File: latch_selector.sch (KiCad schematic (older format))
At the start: 15 parts, among them SW1 SW_Coded_Octal-8, U1 74HCT138, U2 74HCT151, U6 74HCT32

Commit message: added diode-AND to unused latch select pins
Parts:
- removed D1: BAT54AW, Package_TO_SOT_SMD:SOT-323_SC-70, symbol Diode:BAT54AW
- added D1: SD103ATW, Package_TO_SOT_SMD:SOT-363_SC-70-6, symbol Diode:SD103ATW
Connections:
- wire segments 66 -> 65
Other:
- moved on the sheet: RN1
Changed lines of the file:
@@
-	1    0    0    -1
-$EndComp
-$Comp
-L rc2014_monitor-rescue:74HCT138-74xx U?
-U 1 1 5CC19E52
-P 2650 1700
-AR Path="/5CC19E52" Ref="U?"  Part="1"
-AR Path="/5CBDBC11/5CC19E52" Ref="U1"  Part="1"
-F 0 "U1" H 2650 1750 50  0000 C CNN
-F 1 "74HCT138" H 2600 1650 50  0000 C CNN
-F 2 "Package_DIP:DIP-16_W7.62mm" H 2650 1700 50  0001 C CNN
-F 3 "http://www.ti.com/lit/ds/symlink/cd74hct138.pdf" H 2650 1700 50  0001 C CNN
-F 4 "Texas Instruments" H -850 -2150 50  0001 C CNN "MFR"
-F 5 "SN74HCT138N" H -850 -2150 50  0001 C CNN "MPN"
-F 6 "Mouser" H -850 -2150 50  0001 C CNN "SPR"
-F 7 "595-SN74HCT138N" H -850 -2150 50  0001 C CNN "SPN"
-F 8 "-" H -850 -2150 50  0001 C CNN "SPURL"
-	1    2650 1700
 	1    0    0    -1
 $EndComp
@@
 M_WR
 Wire Wire Line
-	4000 1400 4200 1400
-Wire Wire Line
-	4000 1500 4200 1500
-Wire Wire Line
-	4000 1600 4200 1600
-Wire Wire Line
-	4000 1700 4200 1700
-Wire Wire Line
-	4000 1800 4200 1800
-Wire Wire Line
 	2650 1000 2650 1100
 Wire Wire Line
@@
 	2000 4850 2650 4850
 Wire Wire Line
-	4700 1400 4600 1400
+	4800 1400 4700 1400
 Wire Wire Line
 	2050 1000 2050 1900
@@
 Wire Wire Line
 	900  4350 2150 4350
-Wire Wire Line
-	2150 2000 2150 2100
-Wire Wire Line
-	2150 2400 2150 2100
 Connection ~ 2650 1000
 Connection ~ 2000 3850
@@
 Connection ~ 2000 4550
 Connection ~ 2650 4850
-Connection ~ 2650 2400
-Connection ~ 2150 2100
 NoConn ~ 3150 3250
 Wire Wire Line
@@
 L Device:R_Network08 RN?
 U 1 1 5CC19EA4
-P 4400 1800
+P 4500 1800
 AR Path="/5CC19EA4" Ref="RN?"  Part="1"
 AR Path="/5CBDBC11/5CC19EA4" Ref="RN1"  Part="1"
-F 0 "RN1" V 3783 1800 50  0000 C CNN
-F 1 "270R Bussed" V 3874 1800 50  0000 C CNN
-F 2 "Resistor_THT:R_Array_SIP9" V 4875 1800 50  0001 C CNN
-F 3 "https://www.mouser.com/datasheet/2/54/600x-776645.pdf" H 4400 1800 50  0001 C CNN
-F 4 "Bourns" V 4400 1800 50  0001 C CNN "MFR"
-F 5 "4609X-101-271LF" V 4400 1800 50  0001 C CNN "MPN"
-F 6 "Mouser" V 4400 1800 50  0001 C CNN "SPR"
-F 7 "652-4609X-1LF-270" V 4400 1800 50  0001 C CNN "SPN"
-F 8 "https://www.mouser.com/ProductDetail/652-4609X-1LF-270" V 4400 1800 50  0001 C CNN "SPURL"
-	1    4400 1800
+F 0 "RN1" V 3883 1800 50  0000 C CNN
+F 1 "270R Bussed" V 3974 1800 50  0000 C CNN
+F 2 "Resistor_THT:R_Array_SIP9" V 4975 1800 50  0001 C CNN
+F 3 "https://www.mouser.com/datasheet/2/54/600x-776645.pdf" H 4500 1800 50  0001 C CNN
+F 4 "Bourns" V 4500 1800 50  0001 C CNN "MFR"
+F 5 "4609X-101-271LF" V 4500 1800 50  0001 C CNN "MPN"
+F 6 "Mouser" V 4500 1800 50  0001 C CNN "SPR"
+F 7 "652-4609X-1LF-270" V 4500 1800 50  0001 C CNN "SPN"
+F 8 "https://www.mouser.com/ProductDetail/652-4609X-1LF-270" V 4500 1800 50  0001 C CNN "SPURL"
+	1    4500 1800
 	0    1    1    0
 $EndComp
-NoConn ~ 4200 2000
-NoConn ~ 4200 2100
+NoConn ~ 4300 2000
+NoConn ~ 4300 2100
 $Comp
 L Device:LED_Small LED?
@@
 	1    0    0    -1
 $EndComp
-Wire Wire Line
-	4000 1900 4200 1900
 Text Notes 3650 1900 0    50   ~ 0
 5V
-Wire Wire Line
-	3150 2100 3200 2100
 $Comp
 L rc2014_monitor-rescue:74HCT32-74xx U?
@@
 	5400 3300 5850 3300
 Wire Wire Line
-	3600 1900 3800 1900
-Wire Wire Line
 	5400 3750 5400 3600
 Wire Wire Line
 	5400 3150 5400 3300
 Wire Wire Line
-	4700 1000 4700 1400
-Wire Wire Line
-	2650 1000 4700 1000
+	4800 1000 4800 1400
 Wire Wire Line
 	3150 1800 3800 1800
-$Comp
-L Diode:BAT54AW D1
-U 1 1 5CCA392F
-P 3400 2300
-F 0 "D1" V 3446 2388 50  0000 L CNN
-F 1 "BAT54AW" V 3355 2388 50  0000 L CNN
-F 2 "Package_TO_SOT_SMD:SOT-323_SC-70" H 3475 2425 50  0001 L CNN
-F 3 "https://assets.nexperia.com/documents/data-sheet/BAT54W_SER.pdf" H 3280 2300 50  0001 C CNN
-	1    3400 2300
-	0    -1   -1   0
-$EndComp
-Wire Wire Line
-	3600 1900 3600 2300
-Wire Wire Line
-	3150 1900 3600 1900
-Connection ~ 3600 1900
-Wire Wire Line
-	3150 2000 3400 2000
-Wire Wire Line
-	3200 2100 3200 2600
-Wire Wire Line
-	3200 2600 3400 2600
 Wire Wire Line
 	3150 1700 3800 1700
@@
 Wire Wire Line
 	3150 1400 3800 1400
+Connection ~ 2650 2400
+Wire Wire Line
+	2150 2400 2150 2100
+Wire Wire Line
+	2150 2000 2150 2100
+Connection ~ 2150 2100
+$Comp
+L rc2014_monitor-rescue:74HCT138-74xx U?
+U 1 1 5CC19E52
+P 2650 1700
+AR Path="/5CC19E52" Ref="U?"  Part="1"
+AR Path="/5CBDBC11/5CC19E52" Ref="U1"  Part="1"
+F 0 "U1" H 2650 1750 50  0000 C CNN
+F 1 "74HCT138" H 2600 1650 50  0000 C CNN
+F 2 "Package_DIP:DIP-16_W7.62mm" H 2650 1700 50  0001 C CNN
+F 3 "http://www.ti.com/lit/ds/symlink/cd74hct138.pdf" H 2650 1700 50  0001 C CNN
+F 4 "Texas Instruments" H -850 -2150 50  0001 C CNN "MFR"
+F 5 "SN74HCT138N" H -850 -2150 50  0001 C CNN "MPN"
+F 6 "Mouser" H -850 -2150 50  0001 C CNN "SPR"
+F 7 "595-SN74HCT138N" H -850 -2150 50  0001 C CNN "SPN"
+F 8 "-" H -850 -2150 50  0001 C CNN "SPURL"
+	1    2650 1700
+	1    0    0    -1
+$EndComp
+Wire Wire Line
+	4000 1400 4300 1400
+Wire Wire Line
+	4000 1500 4300 1500
+Wire Wire Line
+	4000 1600 4300 1600
+Wire Wire Line
+	4000 1700 4300 1700
+Wire Wire Line
+	4000 1800 4300 1800
+Wire Wire Line
+	4000 1900 4300 1900
+$Comp
+L Diode:SD103ATW D1
+U 1 1 5CB2381C
+P 3500 1900
+F 0 "D1" H 3500 1550 50  0000 C CNN
+F 1 "SD103ATW" H 3500 1450 50  0000 C CNN
+F 2 "Package_TO_SOT_SMD:SOT-363_SC-70-6" H 3500 1700 50  0001 C CNN
+F 3 "https://www.mouser.com/datasheet/2/115/ds30374-80918.pdf" H 3500 1900 50  0001 C CNN
+F 4 "Diodes Incorporated" H 3500 1900 50  0001 C CNN "MFR"
+F 5 "SD103ATW-7-F" H 3500 1900 50  0001 C CNN "MPN"
+F 6 "Mouser" H 3500 1900 50  0001 C CNN "SPR"
+F 7 "621-SD103ATW-F" H 3500 1900 50  0001 C CNN "SPN"
+	1    3500 1900
+	1    0    0    -1
+$EndComp
+$Comp
+L Diode:SD103ATW D1
+U 2 1 5CB2450A
+P 3500 2100
+F 0 "D1" H 3500 1650 50  0000 C CNN
+F 1 "SD103ATW" H 3500 1550 50  0000 C CNN
+F 2 "Package_TO_SOT_SMD:SOT-363_SC-70-6" H 3500 1900 50  0001 C CNN
+F 3 "https://www.mouser.com/datasheet/2/115/ds30374-80918.pdf" H 3500 2100 50  0001 C CNN
+	2    3500 2100
+	1    0    0    -1
+$EndComp
+$Comp
+L Diode:SD103ATW D1
+U 3 1 5CB253E2
+P 3500 2000
+F 0 "D1" H 3500 1500 50  0000 C CNN
+F 1 "SD103ATW" H 3500 1400 50  0000 C CNN
+F 2 "Package_TO_SOT_SMD:SOT-363_SC-70-6" H 3500 1800 50  0001 C CNN
+F 3 "https://www.mouser.com/datasheet/2/115/ds30374-80918.pdf" H 3500 2000 50  0001 C CNN
+	3    3500 2000
+	1    0    0    -1
+$EndComp
+Wire Wire Line
+	3150 1900 3350 1900
+Wire Wire Line
+	3150 2000 3350 2000
+Wire Wire Line
+	3150 2100 3350 2100
+Wire Wire Line
+	3650 2000 3650 2100
+Wire Wire Line
+	3650 1900 3800 1900
+Wire Wire Line
+	2650 1000 4800 1000
+Wire Wire Line
+	3650 2000 3650 1900
+Connection ~ 3650 2000
+Connection ~ 3650 1900
 $EndSCHEMATC

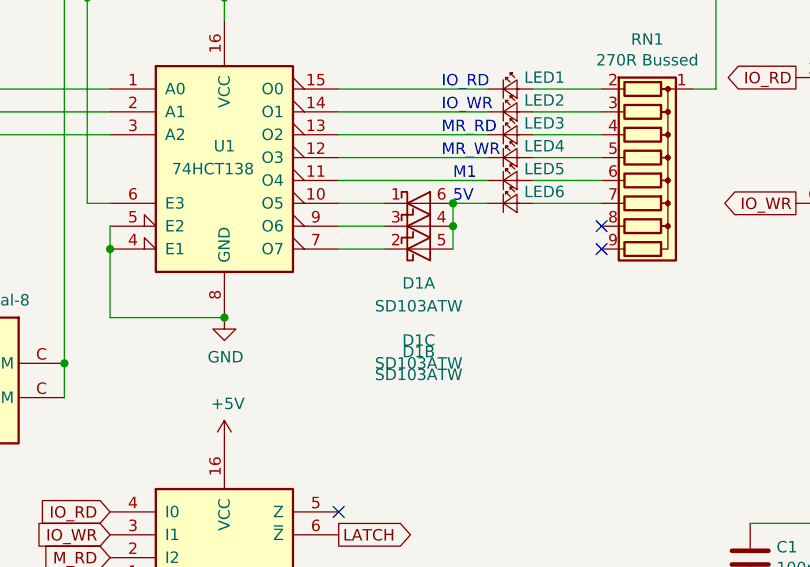
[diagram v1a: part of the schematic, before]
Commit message: added pro bus, generated gerbers
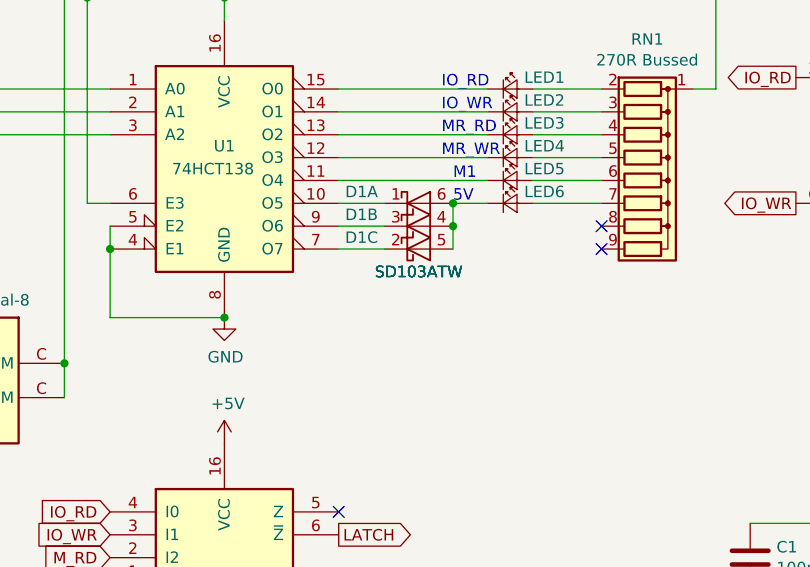
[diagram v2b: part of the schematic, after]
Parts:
- D1: SPURL (none) -> https://www.mouser.com/ProductDetail/Diodes-Incorporated/SD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
- D1: MFR (none) -> Diodes Incorporated; MPN (none) -> SD103ATW-7-F; SPN (none) -> 621-SD103ATW-F; SPR (none) -> Mouser; SPURL (none) -> https://www.mouser.com/ProductDetail/Diodes-Incorporated/SD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
- U1, U2: footprint Package_DIP:DIP-16_W7.62mm -> Package_DIP:DIP-16_W7.62mm_Socket
- U6: footprint Package_DIP:DIP-14_W7.62mm -> Package_DIP:DIP-14_W7.62mm_Socket
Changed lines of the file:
@@
 F 0 "U6" H 6600 1675 50  0000 C CNN
 F 1 "74HCT32" H 6600 1584 50  0000 C CNN
-F 2 "Package_DIP:DIP-14_W7.62mm" H 6600 1350 50  0001 C CNN
+F 2 "Package_DIP:DIP-14_W7.62mm_Socket" H 6600 1350 50  0001 C CNN
 F 3 "http://www.ti.com/lit/ds/symlink/sn74hct32.pdf" H 6600 1350 50  0001 C CNN
 F 4 "Texas Instruments" H 400 -3800 50  0001 C CNN "MFR"
@@
 F 0 "U6" H 6600 2225 50  0000 C CNN
 F 1 "74HCT32" H 6600 2134 50  0000 C CNN
-F 2 "Package_DIP:DIP-14_W7.62mm" H 6600 1900 50  0001 C CNN
+F 2 "Package_DIP:DIP-14_W7.62mm_Socket" H 6600 1900 50  0001 C CNN
 F 3 "http://www.ti.com/lit/ds/symlink/sn74hct32.pdf" H 6600 1900 50  0001 C CNN
 F 4 "Texas Instruments" H 400 -3800 50  0001 C CNN "MFR"
@@
 F 0 "U6" H 5450 2225 50  0000 C CNN
 F 1 "74HCT32" H 5450 2134 50  0000 C CNN
-F 2 "Package_DIP:DIP-14_W7.62mm" H 5450 1900 50  0001 C CNN
+F 2 "Package_DIP:DIP-14_W7.62mm_Socket" H 5450 1900 50  0001 C CNN
 F 3 "http://www.ti.com/lit/ds/symlink/sn74hct32.pdf" H 5450 1900 50  0001 C CNN
 F 4 "Texas Instruments" H 400 -3800 50  0001 C CNN "MFR"
@@
 F 0 "U6" H 5450 1675 50  0000 C CNN
 F 1 "74HCT32" H 5450 1584 50  0000 C CNN
-F 2 "Package_DIP:DIP-14_W7.62mm" H 5450 1350 50  0001 C CNN
+F 2 "Package_DIP:DIP-14_W7.62mm_Socket" H 5450 1350 50  0001 C CNN
 F 3 "http://www.ti.com/lit/ds/symlink/sn74hct32.pdf" H 5450 1350 50  0001 C CNN
 F 4 "Texas Instruments" H 400 -3800 50  0001 C CNN "MFR"
@@
 F 0 "U2" H 2650 3900 50  0000 C CNN
 F 1 "74HCT151" H 2700 3750 50  0000 C CNN
-F 2 "Package_DIP:DIP-16_W7.62mm" H 2650 3850 50  0001 C CNN
+F 2 "Package_DIP:DIP-16_W7.62mm_Socket" H 2650 3850 50  0001 C CNN
 F 3 "http://www.ti.com/lit/ds/symlink/cd74hct151.pdf" H 2650 3850 50  0001 C CNN
 F 4 "Texas Instruments" H -850 -2150 50  0001 C CNN "MFR"
@@
 F 0 "U6" H 7880 1696 50  0000 L CNN
 F 1 "74HCT32" H 7880 1605 50  0000 L CNN
-F 2 "Package_DIP:DIP-14_W7.62mm" H 7650 1650 50  0001 C CNN
+F 2 "Package_DIP:DIP-14_W7.62mm_Socket" H 7650 1650 50  0001 C CNN
 F 3 "http://www.ti.com/lit/ds/symlink/sn74hct32.pdf" H 7650 1650 50  0001 C CNN
 F 4 "Texas Instruments" H 150 -4000 50  0001 C CNN "MFR"
@@
 F 0 "U1" H 2650 1750 50  0000 C CNN
 F 1 "74HCT138" H 2600 1650 50  0000 C CNN
-F 2 "Package_DIP:DIP-16_W7.62mm" H 2650 1700 50  0001 C CNN
+F 2 "Package_DIP:DIP-16_W7.62mm_Socket" H 2650 1700 50  0001 C CNN
 F 3 "http://www.ti.com/lit/ds/symlink/cd74hct138.pdf" H 2650 1700 50  0001 C CNN
 F 4 "Texas Instruments" H -850 -2150 50  0001 C CNN "MFR"
@@
 U 1 1 5CB2381C
 P 3500 1900
-F 0 "D1" H 3500 1550 50  0000 C CNN
-F 1 "SD103ATW" H 3500 1450 50  0000 C CNN
+F 0 "D1" H 3250 1950 50  0000 C CNN
+F 1 "SD103ATW" H 3500 1600 50  0000 C CNN
 F 2 "Package_TO_SOT_SMD:SOT-363_SC-70-6" H 3500 1700 50  0001 C CNN
 F 3 "https://www.mouser.com/datasheet/2/115/ds30374-80918.pdf" H 3500 1900 50  0001 C CNN
@@
 F 6 "Mouser" H 3500 1900 50  0001 C CNN "SPR"
 F 7 "621-SD103ATW-F" H 3500 1900 50  0001 C CNN "SPN"
+F 8 "https://www.mouser.com/ProductDetail/Diodes-Incorporated/SD103ATW-7-F?qs=%2Fha2pyFadugDGjjBrIiZL0DOY1Gy23gp1dHZHpATh%2FKBhtYLvEjSow%3D%3D" H 0   0   50  0001 C CNN "SPURL"
 	1    3500 1900
 	1    0    0    -1
@@
 U 2 1 5CB2450A
 P 3500 2100
-F 0 "D1" H 3500 1650 50  0000 C CNN
-F 1 "SD103ATW" H 3500 1550 50  0000 C CNN
+F 0 "D1" H 3250 2250 50  0000 C CNN
+F 1 "SD103ATW" H 3500 2000 50  0000 C CNN
 F 2 "Package_TO_SOT_SMD:SOT-363_SC-70-6" H 3500 1900 50  0001 C CNN
 F 3 "https://www.mouser.com/datasheet/2/115/ds30374-80918.pdf" H 3500 2100 50  0001 C CNN
+F 4 "Diodes Incorporated" H 0   0   50  0001 C CNN "MFR"
+F 5 "SD103ATW-7-F" H 0   0   50  0001 C CNN "MPN"
+F 6 "621-SD103ATW-F" H 0   0   50  0001 C CNN "SPN"
+F 7 "Mouser" H 0   0   50  0001 C CNN "SPR"
+F 8 "https://www.mouser.com/ProductDetail/Diodes-Incorporated/SD103ATW-7-F?qs=%2Fha2pyFadugDGjjBrIiZL0DOY1Gy23gp1dHZHpATh%2FKBhtYLvEjSow%3D%3D" H 0   0   50  0001 C CNN "SPURL"
 	2    3500 2100
 	1    0    0    -1
@@
 U 3 1 5CB253E2
 P 3500 2000
-F 0 "D1" H 3500 1500 50  0000 C CNN
-F 1 "SD103ATW" H 3500 1400 50  0000 C CNN
+F 0 "D1" H 3250 1950 50  0000 C CNN
+F 1 "SD103ATW" H 3500 1800 50  0000 C CNN
 F 2 "Package_TO_SOT_SMD:SOT-363_SC-70-6" H 3500 1800 50  0001 C CNN
 F 3 "https://www.mouser.com/datasheet/2/115/ds30374-80918.pdf" H 3500 2000 50  0001 C CNN
+F 4 "Diodes Incorporated" H 0   0   50  0001 C CNN "MFR"
+F 5 "SD103ATW-7-F" H 0   0   50  0001 C CNN "MPN"
+F 6 "621-SD103ATW-F" H 0   0   50  0001 C CNN "SPN"
+F 7 "Mouser" H 0   0   50  0001 C CNN "SPR"
+F 8 "https://www.mouser.com/ProductDetail/Diodes-Incorporated/SD103ATW-7-F?qs=%2Fha2pyFadugDGjjBrIiZL0DOY1Gy23gp1dHZHpATh%2FKBhtYLvEjSow%3D%3D" H 0   0   50  0001 C CNN "SPURL"
 	3    3500 2000
 	1    0    0    -1

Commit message: label updates
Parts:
- SW1: value SW_Coded_Octal-8 -> Line Selection
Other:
- moved on the sheet: C1, C2, C6, D1A, D1B, D1C, LED1, LED2, LED3, LED4, LED5, LED6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

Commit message: Changed display buffer and other parts
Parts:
- added C11, C12: 10nF, Capacitor_SMD:C_0805_2012Metric_Pad1.15x1.40mm_HandSolder, symbol Device:C
- added C13, C14: 100nF, Capacitor_SMD:C_0805_2012Metric_Pad1.15x1.40mm_HandSolder, symbol Device:C
- added RN2: 10K, Resistor_THT:R_Array_SIP6, symbol Device:R_Network05
- added SW3: Step, Button_Switch_THT:SW_NKK_BB15AH, symbol Switch:SW_Push_SPDT
- added SW4: Run/Step Mode, Button_Switch_THT:SW_NKK_BB15AH, symbol Switch:SW_SPDT
- added U10: LMC555xM, Package_SO:SOIC-8_3.9x4.9mm_P1.27mm, symbol Timer:LMC555xM
- added U11: 74HCT00, Package_DIP:DIP-14_W7.62mm, symbol 74xx:74HCT00
- added U12: 74HCT74, Package_DIP:DIP-14_W7.62mm, symbol 74xx:74HCT74
- C1, C2, C6: footprint Capacitor_THT:C_Disc_D5.0mm_W2.5mm_P2.50mm -> Capacitor_SMD:C_0805_2012Metric_Pad1.15x1.40mm_HandSolder; MFR Vishay -> KEMET; MPN 1C10Z5U104M050R -> C0805C104K4RACTU; SPN 75-1C10Z5U104M050R -> 80-C0805C104K4R; SPURL - -> https://www.mouser.com/ProductDetail/KEMET/C0805C104K4RACTU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
- D1: value SD103ATW -> CMXSH-3 TR; footprint Package_TO_SOT_SMD:SOT-363_SC-70-6 -> Package_TO_SOT_SMD:SOT-23-6_Handsoldering; MFR Diodes Incorporated -> Central Semiconductor; MPN SD103ATW-7-F -> CMXSH-3 TR; SPN 621-SD103ATW-F -> 610-CMXSH-3; SPURL https://www.mouser.com/ProductDetail/Diodes-Incorporated/SD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 -> https://www.mouser.com/ProductDetail/610-CMXSH-3
- U1: footprint Package_DIP:DIP-16_W7.62mm_Socket -> Package_DIP:DIP-16_W7.62mm; MPN SN74HCT138N -> CD74HCT138E; SPN 595-SN74HCT138N -> 595-CD74HCT138E; SPURL - -> https://www.mouser.com/ProductDetail/Texas-Instruments/CD74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
- U2: footprint Package_DIP:DIP-16_W7.62mm_Socket -> Package_DIP:DIP-16_W7.62mm; SPURL - -> https://www.mouser.com/ProductDetail/Texas-Instruments/CD74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
- U6: footprint Package_DIP:DIP-14_W7.62mm_Socket -> Package_DIP:DIP-14_W7.62mm; MPN SN74HCT32N -> CD74HCT32E; SPN 595-SN74HCT32N -> 595-CD74HCT32E; SPURL - -> https://www.mouser.com/ProductDetail/Texas-Instruments/CD74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
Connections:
- net +5V: now also C13.1, C14.1, RN2.1 (common), U10.8 (VCC), U11.14 (VCC), U12.14 (VCC)
- net GND: now also C11.2, C12.2, C13.2, C14.2, SW3.2 (B), SW4.2 (B), U10.1 (GND), U11.12, U11.13, U11.7 (GND), U12.10 (~S), U12.11 (C), U12.12 (D), U12.13 (~R), U12.4 (~S), U12.7 (GND)
- net ~M1: now also U10.2 (TR), U10.4 (R)
- new net: U11.2, U11.6, U12.3 (C)
- new net: U11.3, U11.4
- new net: U11.9, U12.6 (~Q)
- new net: U10.3 (Q), U12.1 (~R)
- new net: C11.1, U10.5 (CV)
- new net R5: SW4.1 (A), U11.10
- new net U10_7: C12.1, RN2.5 (R4), U10.6 (THR), U10.7 (DIS)
- new net U11A_1: RN2.2 (R1), SW3.1 (A), U11.1
- new net U11A_5: RN2.3 (R2), SW3.3 (C), U11.5
- new net U11C_10: RN2.6 (R5)
- new net U12A_2: RN2.4 (R3), U12.2 (D)
- new net ~WAIT: U11.8
- no-connect marks 3 -> 8
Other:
- note added: "Instruction Stepper"
- note added: "Run"
- note added: "Step"
- moved on the sheet: C1, C2, C6, D1A, D1B, D1C, LED1, LED2, LED3, LED4, LED5, LED6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

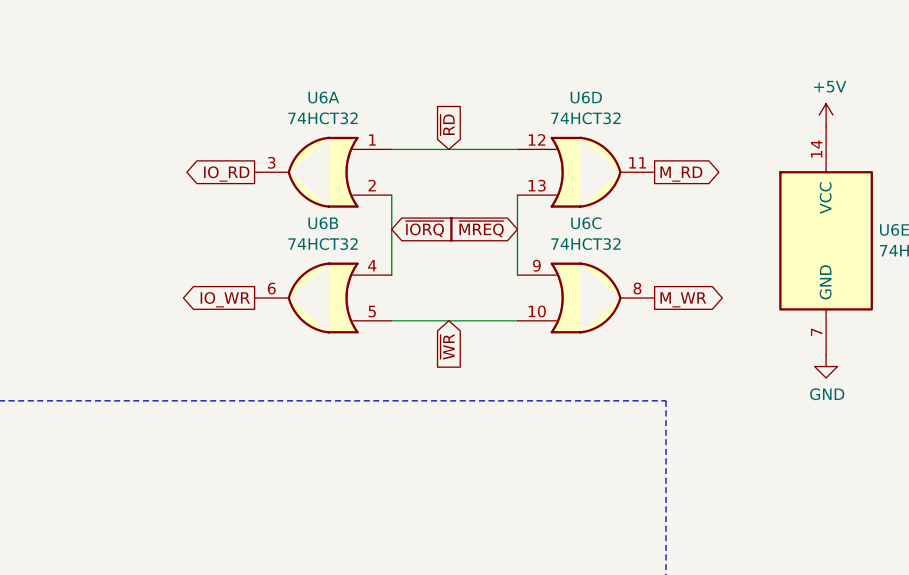
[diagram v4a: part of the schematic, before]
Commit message: added single stepping, changed routing and placement
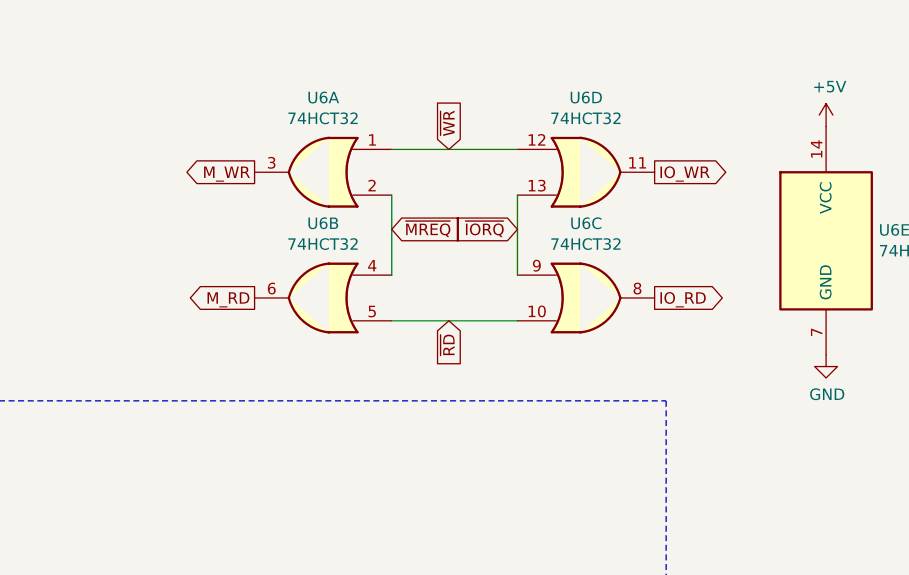
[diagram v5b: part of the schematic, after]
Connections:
- net IO_RD: now also U6.8; no longer U6.3
- net IO_WR: now also U6.11; no longer U6.6
- net M_RD: now also U6.6; no longer U6.11
- net M_WR: now also U6.3; no longer U6.8
- net ~IORQ: now also U6.13, U6.9; no longer U6.2, U6.4
- net ~MREQ: now also U6.2, U6.4; no longer U6.13, U6.9
- net ~RD: now also U6.10, U6.5; no longer U6.1, U6.12
- net ~WR: now also U6.1, U6.12; no longer U6.10, U6.5
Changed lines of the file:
@@
 	-1   0    0    -1
 $EndComp
+Text GLabel 3700 1100 0    50   Output ~ 0
+M_WR
+Text GLabel 3700 1650 0    50   Output ~ 0
+M_RD
+Text GLabel 5450 1100 2    50   Output ~ 0
+IO_WR
 Text GLabel 5450 1650 2    50   Output ~ 0
-M_WR
-Text GLabel 5450 1100 2    50   Output ~ 0
-M_RD
-Text GLabel 3700 1650 0    50   Output ~ 0
-IO_WR
-Text GLabel 3700 1100 0    50   Output ~ 0
 IO_RD
+Text GLabel 4300 1350 2    50   Input ~ 0
+~MREQ
+Text GLabel 4550 1000 1    50   Input ~ 0
+~WR
+Text GLabel 4550 1750 3    50   Input ~ 0
+~RD
 Text GLabel 4850 1350 0    50   Input ~ 0
-~MREQ
-Text GLabel 4550 1750 3    50   Input ~ 0
-~WR
-Text GLabel 4550 1000 1    50   Input ~ 0
-~RD
-Text GLabel 4300 1350 2    50   Input ~ 0
 ~IORQ
 Wire Wire Line

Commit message: more routing
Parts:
- U12: symbol 74xx:74HCT74 -> rc2014_monitor-rescue:74HCT74-74xx
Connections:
- net R5 is gone; now on net U11C_10: SW4.1 (A), U11.10
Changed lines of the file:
@@
 $EndComp
 $Comp
-L 74xx:74HCT74 U12
+L rc2014_monitor-rescue:74HCT74-74xx U12
 U 1 1 5CBB2D0A
 P 3500 3550
+AR Path="/5CBB2D0A" Ref="U12"  Part="1"
+AR Path="/5CBDBC11/5CBB2D0A" Ref="U12"  Part="1"
 F 0 "U12" H 3500 3550 50  0000 C CNN
 F 1 "74HCT74" H 3150 3400 50  0000 C CNN
@@
 $EndComp
 $Comp
-L 74xx:74HCT74 U12
+L rc2014_monitor-rescue:74HCT74-74xx U12
 U 2 1 5CBB3EEE
 P 1750 6800
+AR Path="/5CBB3EEE" Ref="U12"  Part="2"
+AR Path="/5CBDBC11/5CBB3EEE" Ref="U12"  Part="2"
 F 0 "U12" H 1750 7281 50  0000 C CNN
 F 1 "74HCT74" H 1750 7190 50  0000 C CNN
@@
 $EndComp
 $Comp
-L 74xx:74HCT74 U12
+L rc2014_monitor-rescue:74HCT74-74xx U12
 U 3 1 5CBB6803
 P 3550 6350
+AR Path="/5CBB6803" Ref="U12"  Part="3"
+AR Path="/5CBDBC11/5CBB6803" Ref="U12"  Part="3"
 F 0 "U12" H 3780 6396 50  0000 L CNN
 F 1 "74HCT74" H 3780 6305 50  0000 L CNN
@@
 U11A_5
 Text GLabel 4350 4050 0    50   Input ~ 0
-R5
+U11C_10
 Wire Wire Line
 	4350 3850 4350 4500
